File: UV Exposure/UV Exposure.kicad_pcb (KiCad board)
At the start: 2 copper layers, 102 x 90 mm, 94 parts, among them P1 Conn_01x01, P2 Conn_01x01

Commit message: update PCB track
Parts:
- removed REF** (x2): Pin_D1.0mm_L10.0mm, Connector_Pin:Pin_D1.0mm_L10.0mm
- added +12V: POWER, Connector_Pin:Pin_D1.0mm_L10.0mm, F.Cu at (176.0, 109.2)
- added +12V: POWER, Connector_Pin:Pin_D1.0mm_L10.0mm, F.Cu at (52.1, 109.2)
- added D1: LED, LED_THT:LED_D5.0mm, F.Cu at (169.6, 38.1)
- added D10: LED, LED_THT:LED_D5.0mm, F.Cu at (182.3, 76.2)
- added D11: LED, LED_THT:LED_D5.0mm, F.Cu at (182.3, 88.9)
- added D12: LED, LED_THT:LED_D5.0mm, F.Cu at (182.3, 101.6)
- added D13: LED, LED_THT:LED_D5.0mm, F.Cu at (195.3, 38.1)
- added D14: LED, LED_THT:LED_D5.0mm, F.Cu at (195.3, 50.8)
- added D15: LED, LED_THT:LED_D5.0mm, F.Cu at (195.3, 63.5)
- added D16: LED, LED_THT:LED_D5.0mm, F.Cu at (195.3, 76.2)
- added D17: LED, LED_THT:LED_D5.0mm, F.Cu at (195.3, 88.9)
- added D18: LED, LED_THT:LED_D5.0mm, F.Cu at (195.3, 101.6)
- added D19: LED, LED_THT:LED_D5.0mm, F.Cu at (207.7, 38.1)
- added D2: LED, LED_THT:LED_D5.0mm, F.Cu at (169.6, 50.8)
- added D20: LED, LED_THT:LED_D5.0mm, F.Cu at (207.7, 50.8)
- added D21: LED, LED_THT:LED_D5.0mm, F.Cu at (207.7, 63.5)
- added D22: LED, LED_THT:LED_D5.0mm, F.Cu at (207.7, 76.2)
- added D23: LED, LED_THT:LED_D5.0mm, F.Cu at (207.7, 88.9)
- added D24: LED, LED_THT:LED_D5.0mm, F.Cu at (207.7, 101.6)
- added D25: LED, LED_THT:LED_D5.0mm, F.Cu at (220.4, 38.1)
- added D26: LED, LED_THT:LED_D5.0mm, F.Cu at (220.4, 50.8)
- added D27: LED, LED_THT:LED_D5.0mm, F.Cu at (220.4, 63.5)
- added D28: LED, LED_THT:LED_D5.0mm, F.Cu at (220.4, 76.2)
- added D29: LED, LED_THT:LED_D5.0mm, F.Cu at (220.4, 88.9)
- added D3: LED, LED_THT:LED_D5.0mm, F.Cu at (169.6, 63.5)
- added D30: LED, LED_THT:LED_D5.0mm, F.Cu at (220.4, 101.6)
- added D31: LED, LED_THT:LED_D5.0mm, F.Cu at (233.1, 38.1)
- added D32: LED, LED_THT:LED_D5.0mm, F.Cu at (233.1, 50.8)
- added D33: LED, LED_THT:LED_D5.0mm, F.Cu at (233.1, 63.5)
- added D34: LED, LED_THT:LED_D5.0mm, F.Cu at (233.1, 76.2)
- added D35: LED, LED_THT:LED_D5.0mm, F.Cu at (233.1, 88.9)
- added D36: LED, LED_THT:LED_D5.0mm, F.Cu at (233.1, 101.6)
- added D37: LED, LED_THT:LED_D5.0mm, F.Cu at (245.8, 38.1)
- added D38: LED, LED_THT:LED_D5.0mm, F.Cu at (245.8, 50.5)
- added D39: LED, LED_THT:LED_D5.0mm, F.Cu at (245.8, 63.5)
- added D4: LED, LED_THT:LED_D5.0mm, F.Cu at (169.6, 76.2)
- added D40: LED, LED_THT:LED_D5.0mm, F.Cu at (245.8, 76.2)
- added D41: LED, LED_THT:LED_D5.0mm, F.Cu at (245.8, 88.9)
- added D42: LED, LED_THT:LED_D5.0mm, F.Cu at (245.8, 101.6)
- added D43: LED, LED_THT:LED_D5.0mm, F.Cu at (258.5, 38.1)
- added D44: LED, LED_THT:LED_D5.0mm, F.Cu at (258.5, 50.8)
- added D45: LED, LED_THT:LED_D5.0mm, F.Cu at (258.5, 63.5)
- added D46: LED, LED_THT:LED_D5.0mm, F.Cu at (258.5, 76.2)
- added D47: LED, LED_THT:LED_D5.0mm, F.Cu at (258.5, 88.9)
- added D48: LED, LED_THT:LED_D5.0mm, F.Cu at (258.5, 101.6)
- added D49: LED, LED_THT:LED_D5.0mm, F.Cu at (183.6, 113.0)
- added D5: LED, LED_THT:LED_D5.0mm, F.Cu at (169.6, 88.9)
- added D50: LED, LED_THT:LED_D5.0mm, F.Cu at (196.6, 113.0)
- added D51: LED, LED_THT:LED_D5.0mm, F.Cu at (209.0, 113.0)
- added D52: LED, LED_THT:LED_D5.0mm, F.Cu at (244.6, 113.0)
- added D53: LED, LED_THT:LED_D5.0mm, F.Cu at (231.9, 113.0)
- added D54: LED, LED_THT:LED_D5.0mm, F.Cu at (219.2, 113.0)
- added D6: LED, LED_THT:LED_D5.0mm, F.Cu at (169.6, 101.6)
- added D7: LED, LED_THT:LED_D5.0mm, F.Cu at (182.3, 38.1)
- added D8: LED, LED_THT:LED_D5.0mm, F.Cu at (182.3, 50.8)
- added D9: LED, LED_THT:LED_D5.0mm, F.Cu at (182.3, 63.5)
- added GND: GROUND, Connector_Pin:Pin_D1.0mm_L10.0mm, F.Cu at (252.5, 109.0)
- added GND: GROUND, Connector_Pin:Pin_D1.0mm_L10.0mm, F.Cu at (128.5, 109.0)
- added P1: Conn_01x01, Connector_Pin:Pin_D1.0mm_L10.0mm, F.Cu at (169.7, 112.8)
- added P1: Conn_01x01, Connector_Pin:Pin_D1.0mm_L10.0mm, F.Cu at (176.0, 43.9)
- added P1: Conn_01x01, Connector_Pin:Pin_D1.0mm_L10.0mm, F.Cu at (252.2, 43.9)
- added P1: Conn_01x01, Connector_Pin:Pin_D1.0mm_L10.0mm, F.Cu at (128.3, 43.9)
- added P1: Conn_01x01, Connector_Pin:Pin_D1.0mm_L10.0mm, F.Cu at (52.1, 43.9)
- added P2: Conn_01x01, Connector_Pin:Pin_D1.0mm_L10.0mm, F.Cu at (258.6, 112.8)
- added R1: R, Resistor_SMD:R_0805_2012Metric_Pad1.20x1.40mm_HandSolder, B.Cu at (175.8, 34.5)
- added R10: R, Resistor_SMD:R_0805_2012Metric_Pad1.20x1.40mm_HandSolder, B.Cu at (201.4, 37.8)
- added R11: R, Resistor_SMD:R_0805_2012Metric_Pad1.20x1.40mm_HandSolder, B.Cu at (201.7, 72.6)
- added R12: R, Resistor_SMD:R_0805_2012Metric_Pad1.20x1.40mm_HandSolder, B.Cu at (201.7, 75.9)
- added R13: R, Resistor_SMD:R_0805_2012Metric_Pad1.20x1.40mm_HandSolder, B.Cu at (214.1, 34.5)
- added R14: R, Resistor_SMD:R_0805_2012Metric_Pad1.20x1.40mm_HandSolder, B.Cu at (214.1, 37.8)
- added R15: R, Resistor_SMD:R_0805_2012Metric_Pad1.20x1.40mm_HandSolder, B.Cu at (214.1, 72.6)
- added R16: R, Resistor_SMD:R_0805_2012Metric_Pad1.20x1.40mm_HandSolder, B.Cu at (214.1, 76.2)
- added R17: R, Resistor_SMD:R_0805_2012Metric_Pad1.20x1.40mm_HandSolder, B.Cu at (226.8, 34.5)
- added R18: R, Resistor_SMD:R_0805_2012Metric_Pad1.20x1.40mm_HandSolder, B.Cu at (226.8, 37.8)
- added R19: R, Resistor_SMD:R_0805_2012Metric_Pad1.20x1.40mm_HandSolder, B.Cu at (226.8, 72.6)
- added R2: R, Resistor_SMD:R_0805_2012Metric_Pad1.20x1.40mm_HandSolder, B.Cu at (175.8, 37.8)
- added R20: R, Resistor_SMD:R_0805_2012Metric_Pad1.20x1.40mm_HandSolder, B.Cu at (226.8, 75.9)
- added R21: R, Resistor_SMD:R_0805_2012Metric_Pad1.20x1.40mm_HandSolder, B.Cu at (239.5, 34.5)
- added R22: R, Resistor_SMD:R_0805_2012Metric_Pad1.20x1.40mm_HandSolder, B.Cu at (239.5, 37.8)
- added R23: R, Resistor_SMD:R_0805_2012Metric_Pad1.20x1.40mm_HandSolder, B.Cu at (239.5, 72.6)
- added R24: R, Resistor_SMD:R_0805_2012Metric_Pad1.20x1.40mm_HandSolder, B.Cu at (239.5, 75.9)
- added R25: R, Resistor_SMD:R_0805_2012Metric_Pad1.20x1.40mm_HandSolder, B.Cu at (252.0, 34.5)
- added R26: R, Resistor_SMD:R_0805_2012Metric_Pad1.20x1.40mm_HandSolder, B.Cu at (252.0, 37.8)
- added R27: R, Resistor_SMD:R_0805_2012Metric_Pad1.20x1.40mm_HandSolder, B.Cu at (252.2, 72.6)
- added R28: R, Resistor_SMD:R_0805_2012Metric_Pad1.20x1.40mm_HandSolder, B.Cu at (252.2, 75.9)
- added R29: R, Resistor_SMD:R_0805_2012Metric_Pad1.20x1.40mm_HandSolder, B.Cu at (254.0, 31.8)
- added R3: R, Resistor_SMD:R_0805_2012Metric_Pad1.20x1.40mm_HandSolder, B.Cu at (175.7, 72.6)
- added R30: R, Resistor_SMD:R_0805_2012Metric_Pad1.20x1.40mm_HandSolder, B.Cu at (258.6, 31.8)
- added R31: R, Resistor_SMD:R_0805_2012Metric_Pad1.20x1.40mm_HandSolder, B.Cu at (254.0, 69.6)
- added R32: R, Resistor_SMD:R_0805_2012Metric_Pad1.20x1.40mm_HandSolder, B.Cu at (258.6, 69.6)
- added R33: R, Resistor_SMD:R_0805_2012Metric_Pad1.20x1.40mm_HandSolder, B.Cu at (186.4, 108.0)
- added R34: R, Resistor_SMD:R_0805_2012Metric_Pad1.20x1.40mm_HandSolder, B.Cu at (182.1, 108.0)
- added R35: R, Resistor_SMD:R_0805_2012Metric_Pad1.20x1.40mm_HandSolder, B.Cu at (241.6, 108.0)
- added R36: R, Resistor_SMD:R_0805_2012Metric_Pad1.20x1.40mm_HandSolder, B.Cu at (246.1, 108.0)
- added R4: R, Resistor_SMD:R_0805_2012Metric_Pad1.20x1.40mm_HandSolder, B.Cu at (175.7, 75.9)
- added R5: R, Resistor_SMD:R_0805_2012Metric_Pad1.20x1.40mm_HandSolder, B.Cu at (188.8, 34.5)
- added R6: R, Resistor_SMD:R_0805_2012Metric_Pad1.20x1.40mm_HandSolder, B.Cu at (188.8, 37.8)
- added R7: R, Resistor_SMD:R_0805_2012Metric_Pad1.20x1.40mm_HandSolder, B.Cu at (188.5, 72.6)
- added R8: R, Resistor_SMD:R_0805_2012Metric_Pad1.20x1.40mm_HandSolder, B.Cu at (188.5, 75.9)
- added R9: R, Resistor_SMD:R_0805_2012Metric_Pad1.20x1.40mm_HandSolder, B.Cu at (201.4, 34.5)
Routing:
- net (no net): track 0.00 -> 549.2 mm
- net +12V: track 376.1 -> 752.1 mm
- net GND: track 188.2 -> 376.4 mm
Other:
- board size 102 x 90 mm -> 226 x 90 mm

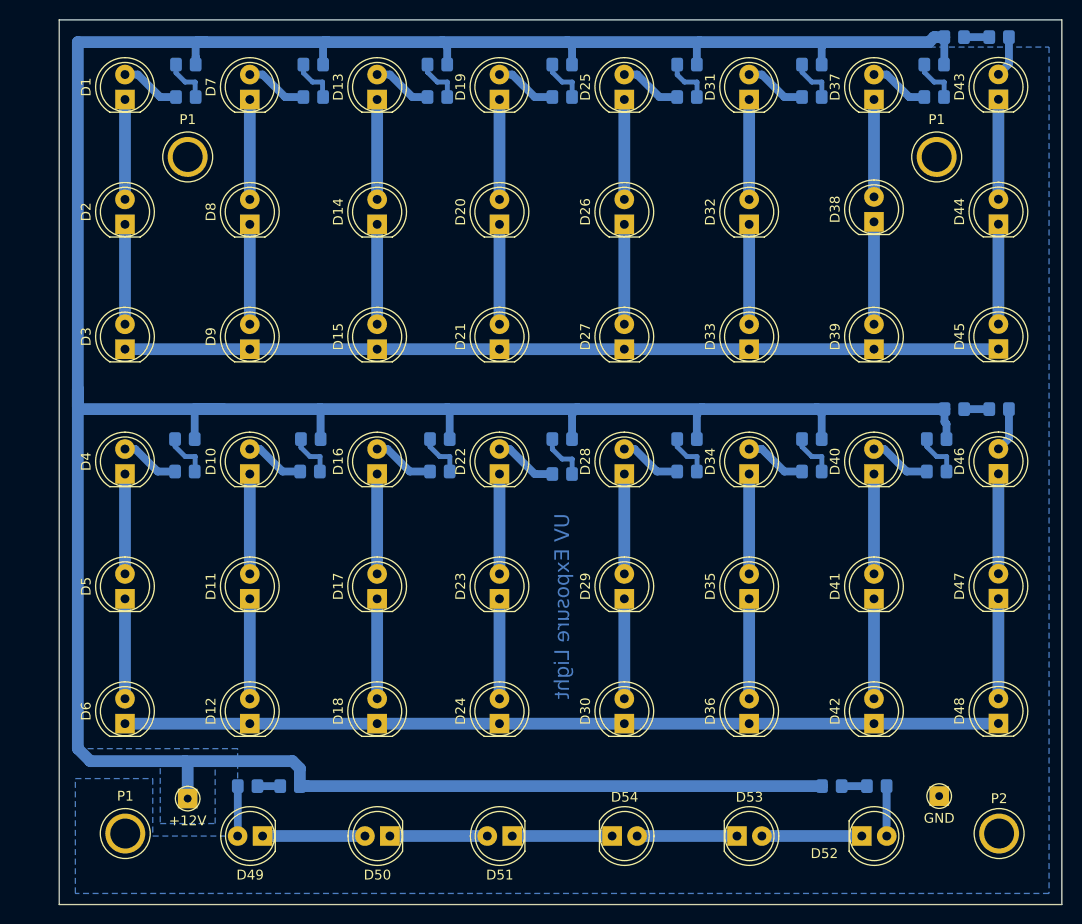
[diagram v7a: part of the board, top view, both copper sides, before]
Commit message: modify logo cancel
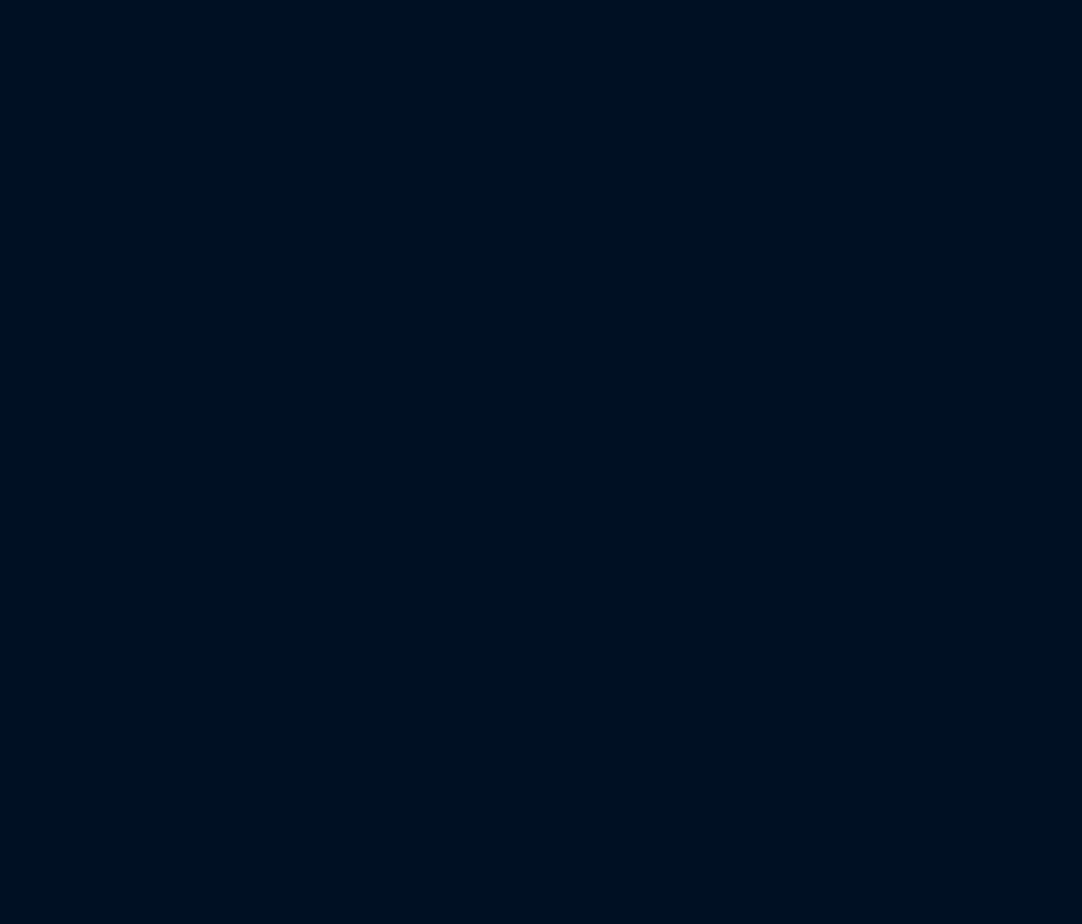
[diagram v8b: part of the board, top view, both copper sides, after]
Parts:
- removed the +12V at (176.0, 109.2)
- removed the D1 at (169.6, 38.1)
- removed the D10 at (182.3, 76.2)
- removed the D11 at (182.3, 88.9)
- removed the D12 at (182.3, 101.6)
- removed the D13 at (195.3, 38.1)
- removed the D14 at (195.3, 50.8)
- removed the D15 at (195.3, 63.5)
- removed the D16 at (195.3, 76.2)
- removed the D17 at (195.3, 88.9)
- removed the D18 at (195.3, 101.6)
- removed the D19 at (207.7, 38.1)
- removed the D2 at (169.6, 50.8)
- removed the D20 at (207.7, 50.8)
- removed the D21 at (207.7, 63.5)
- removed the D22 at (207.7, 76.2)
- removed the D23 at (207.7, 88.9)
- removed the D24 at (207.7, 101.6)
- removed the D25 at (220.4, 38.1)
- removed the D26 at (220.4, 50.8)
- removed the D27 at (220.4, 63.5)
- removed the D28 at (220.4, 76.2)
- removed the D29 at (220.4, 88.9)
- removed the D3 at (169.6, 63.5)
- removed the D30 at (220.4, 101.6)
- removed the D31 at (233.1, 38.1)
- removed the D32 at (233.1, 50.8)
- removed the D33 at (233.1, 63.5)
- removed the D34 at (233.1, 76.2)
- removed the D35 at (233.1, 88.9)
- removed the D36 at (233.1, 101.6)
- removed the D37 at (245.8, 38.1)
- removed the D38 at (245.8, 50.5)
- removed the D39 at (245.8, 63.5)
- removed the D4 at (169.6, 76.2)
- removed the D40 at (245.8, 76.2)
- removed the D41 at (245.8, 88.9)
- removed the D42 at (245.8, 101.6)
- removed the D43 at (258.5, 38.1)
- removed the D44 at (258.5, 50.8)
- removed the D45 at (258.5, 63.5)
- removed the D46 at (258.5, 76.2)
- removed the D47 at (258.5, 88.9)
- removed the D48 at (258.5, 101.6)
- removed the D49 at (183.6, 113.0)
- removed the D5 at (169.6, 88.9)
- removed the D50 at (196.6, 113.0)
- removed the D51 at (209.0, 113.0)
- removed the D52 at (244.6, 113.0)
- removed the D53 at (231.9, 113.0)
- removed the D54 at (219.2, 113.0)
- removed the D6 at (169.6, 101.6)
- removed the D7 at (182.3, 38.1)
- removed the D8 at (182.3, 50.8)
- removed the D9 at (182.3, 63.5)
- removed the GND at (252.5, 109.0)
- removed the P1 at (169.7, 112.8)
- removed the P1 at (176.0, 43.9)
- removed the P1 at (252.2, 43.9)
- removed the P2 at (258.6, 112.8)
- removed the R1 at (175.8, 34.5)
- removed the R10 at (201.4, 37.8)
- removed the R11 at (201.7, 72.6)
- removed the R12 at (201.7, 75.9)
- removed the R13 at (214.1, 34.5)
- removed the R14 at (214.1, 37.8)
- removed the R15 at (214.1, 72.6)
- removed the R16 at (214.1, 76.2)
- removed the R17 at (226.8, 34.5)
- removed the R18 at (226.8, 37.8)
- removed the R19 at (226.8, 72.6)
- removed the R2 at (175.8, 37.8)
- removed the R20 at (226.8, 75.9)
- removed the R21 at (239.5, 34.5)
- removed the R22 at (239.5, 37.8)
- removed the R23 at (239.5, 72.6)
- removed the R24 at (239.5, 75.9)
- removed the R25 at (252.0, 34.5)
- removed the R26 at (252.0, 37.8)
- removed the R27 at (252.2, 72.6)
- removed the R28 at (252.2, 75.9)
- removed the R29 at (254.0, 31.8)
- removed the R3 at (175.7, 72.6)
- removed the R30 at (258.6, 31.8)
- removed the R31 at (254.0, 69.6)
- removed the R32 at (258.6, 69.6)
- removed the R33 at (186.4, 108.0)
- removed the R34 at (182.1, 108.0)
- removed the R35 at (241.6, 108.0)
- removed the R36 at (246.1, 108.0)
- removed the R4 at (175.7, 75.9)
- removed the R5 at (188.8, 34.5)
- removed the R6 at (188.8, 37.8)
- removed the R7 at (188.5, 72.6)
- removed the R8 at (188.5, 75.9)
- removed the R9 at (201.4, 34.5)
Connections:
- P1 pad 1: Net-(P1-Pad1) -> (no net) (x3)
- P2 pad 1: Net-(P2-Pad1) -> (no net)
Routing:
- net (no net): track 549.2 -> 0.00 mm
- net +12V: track 752.1 -> 376.1 mm
- net GND: track 376.4 -> 188.2 mm
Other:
- board size 226 x 90 mm -> 102 x 90 mm
